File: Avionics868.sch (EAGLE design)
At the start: 60 parts, among them SW1 SPST_TACT-KMR2, U1 ATSAMD21G18_QFN, U2 SPX3819M5-L-3-0, U3 MCP73831T-2ACI/OT, U4 MPU-9250, U5 SIM868, U6 BMP180, X1 JSTPH, X2 32.768, X3 microUSB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

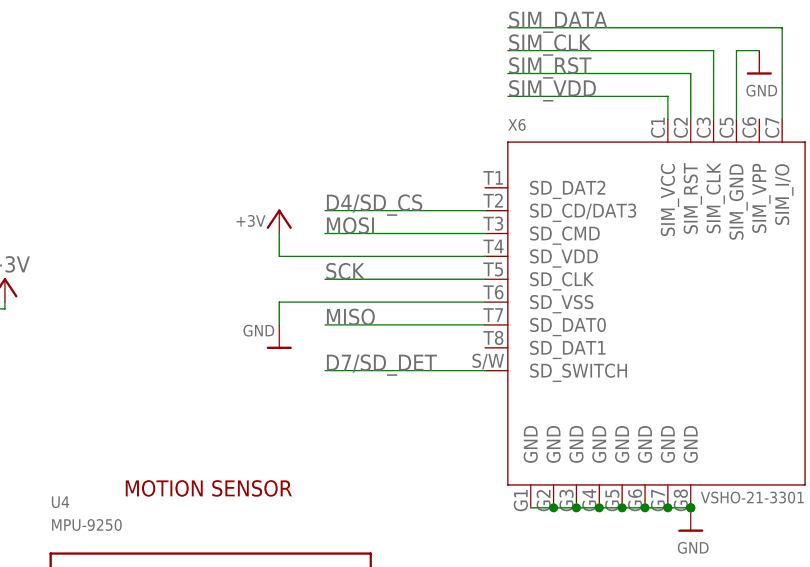
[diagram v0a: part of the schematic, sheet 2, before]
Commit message: Fixed unconnected microsd chip-select
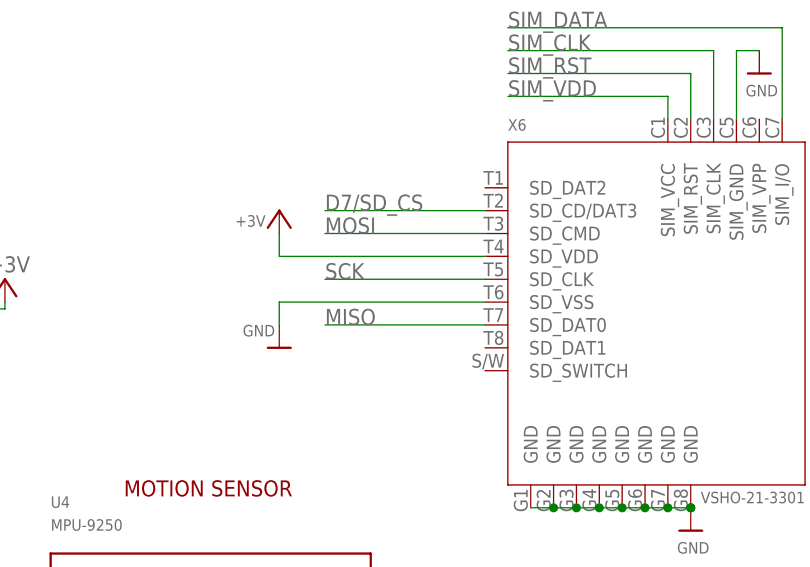
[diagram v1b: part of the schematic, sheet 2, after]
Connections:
- removed net D4/SD_CS: X6.SD_CD/DAT3
- removed net D7/SD_DET: U1.PA21/I5/SERCOM3+5.3/I2SFS0, X6.SD_SWITCH
- new net D7/SD_CS: U1.PA21/I5/SERCOM3+5.3/I2SFS0, X6.SD_CD/DAT3
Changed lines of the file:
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@@
 </segment>
 </net>
-<net name="D7/SD_DET" class="0">
+<net name="D7/SD_CS" class="0">
 <segment>
 <pinref part="U1" gate="G$1" pin="PA21/I5/SERCOM3+5.3/I2SFS0"/>
@@
 </segment>
 </net>
-<net name="D7/SD_DET" class="0">
-<segment>
-<pinref part="X6" gate="G$1" pin="SD_SWITCH"/>
-<wire x1="91.44" y1="83.82" x2="73.66" y2="83.82" width="0.1524" layer="91"/>
-<label x="73.66" y="83.82" size="1.778" layer="95"/>
-</segment>
-</net>
-<net name="D4/SD_CS" class="0">
+<net name="D7/SD_CS" class="0">
 <segment>
 <pinref part="X6" gate="G$1" pin="SD_CD/DAT3"/>

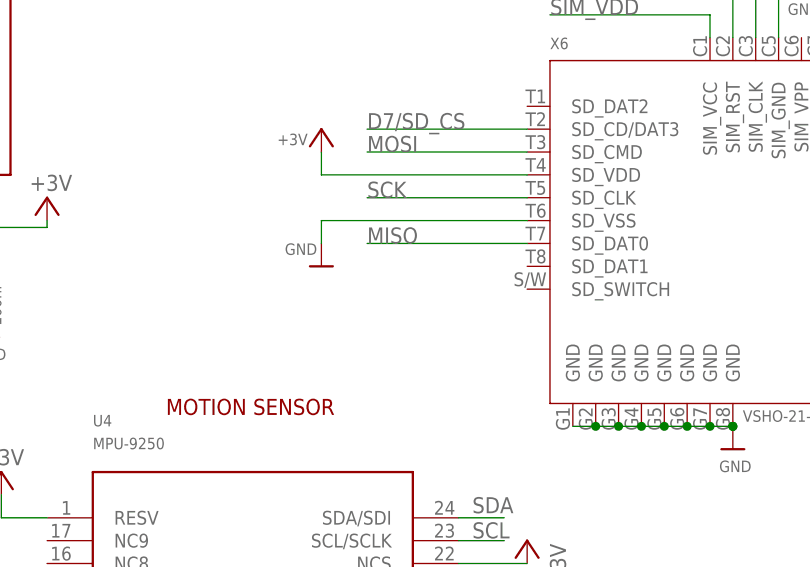
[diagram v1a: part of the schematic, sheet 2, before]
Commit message: Prev. commit was faulty, only half fixed Also fixed a number of ERC/DRC issues
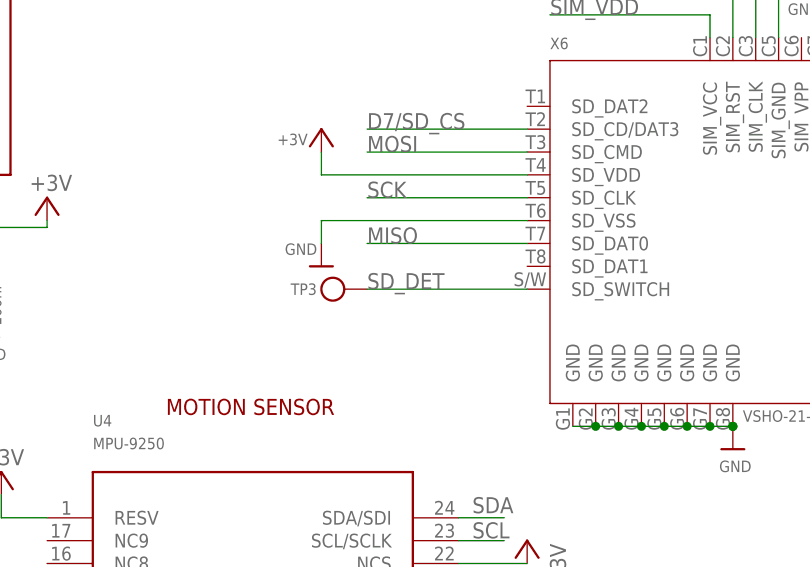
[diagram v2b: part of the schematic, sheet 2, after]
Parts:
- added TP3: (no value), microbuilder:TESTPOINTROUND1.5MM
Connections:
- new net SD_DET: TP3.P$1, X6.SD_SWITCH
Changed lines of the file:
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@@
 <part name="U$2" library="microbuilder" deviceset="VBAT" device=""/>
 <part name="GND13" library="supply1" deviceset="GND" device=""/>
+<part name="TP3" library="microbuilder" deviceset="TESTPOINT" device="ROUND1.5MM"/>
 </parts>
 <sheets>
@@
 <attribute name="VALUE" x="251.968" y="117.729" size="1.27" layer="95" align="center-left"/>
 </instance>
+<instance part="TP3" gate="G$1" x="73.66" y="83.82" rot="R90"/>
 </instances>
 <busses>
@@
 </segment>
 </net>
+<net name="SD_DET" class="0">
+<segment>
+<pinref part="X6" gate="G$1" pin="SD_SWITCH"/>
+<wire x1="91.44" y1="83.82" x2="73.66" y2="83.82" width="0.1524" layer="91"/>
+<pinref part="TP3" gate="G$1" pin="P$1"/>
+<label x="73.66" y="83.82" size="1.778" layer="95"/>
+</segment>
+</net>

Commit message: Added libraries
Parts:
- L3: value ORANGE -> BLUE
- renumbered CHG to L3, L to L1
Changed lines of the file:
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@@
 <part name="GND1" library="supply1" deviceset="GND" device=""/>
 <part name="GND12" library="supply1" deviceset="GND" device=""/>
-<part name="L" library="microbuilder" deviceset="LED" device="0805_NOOUTLINE" value="RED"/>
+<part name="L1" library="microbuilder" deviceset="LED" device="0805_NOOUTLINE" value="RED"/>
 <part name="GND7" library="supply1" deviceset="GND" device=""/>
 <part name="C14" library="microbuilder" deviceset="CAP_CERAMIC" device="0603_NO" value="1uF"/>
@@
 <part name="JP3" library="microbuilder" deviceset="HEADER-1X12" device=""/>
 <part name="U3" library="microbuilder" deviceset="MCP73831/2" device="" value="MCP73831T-2ACI/OT"/>
-<part name="CHG" library="microbuilder" deviceset="LED" device="0805_NOOUTLINE" value="ORANGE"/>
+<part name="L3" library="microbuilder" deviceset="LED" device="0805_NOOUTLINE" value="BLUE"/>
 <part name="R2" library="microbuilder" deviceset="RESISTOR" device="_0603_NOOUT" value="1K"/>
 <part name="C3" library="microbuilder" deviceset="CAP_CERAMIC" device="0805-NOOUTLINE" value="10µF"/>
@@
 <instance part="GND1" gate="1" x="167.64" y="99.06"/>
 <instance part="GND12" gate="1" x="83.82" y="127" rot="MR0"/>
-<instance part="L" gate="G$1" x="246.38" y="50.8" rot="R270"/>
+<instance part="L1" gate="G$1" x="246.38" y="50.8" rot="R270"/>
 <instance part="GND7" gate="1" x="129.54" y="144.78"/>
 <instance part="C14" gate="G$1" x="83.82" y="137.16"/>
@@
 <instance part="JP3" gate="G$1" x="180.34" y="66.04"/>
 <instance part="U3" gate="G$1" x="187.96" y="144.78"/>
-<instance part="CHG" gate="G$1" x="154.94" y="142.24"/>
+<instance part="L3" gate="G$1" x="154.94" y="142.24"/>
 <instance part="R2" gate="G$1" x="165.1" y="142.24"/>
 <instance part="C3" gate="G$1" x="220.98" y="139.7"/>
@@
 </segment>
 <segment>
-<pinref part="L" gate="G$1" pin="C"/>
+<pinref part="L1" gate="G$1" pin="C"/>
 <pinref part="GND10" gate="1" pin="GND"/>
 <wire x1="246.38" y1="48.26" x2="246.38" y2="45.72" width="0.1524" layer="91"/>
@@
 <wire x1="139.7" y1="147.32" x2="147.32" y2="147.32" width="0.1524" layer="91"/>
 <wire x1="147.32" y1="147.32" x2="175.26" y2="147.32" width="0.1524" layer="91"/>
-<pinref part="CHG" gate="G$1" pin="A"/>
+<pinref part="L3" gate="G$1" pin="A"/>
 <wire x1="149.86" y1="142.24" x2="147.32" y2="142.24" width="0.1524" layer="91"/>
 <wire x1="147.32" y1="142.24" x2="147.32" y2="147.32" width="0.1524" layer="91"/>
@@
 <net name="N$2" class="0">
 <segment>
-<pinref part="L" gate="G$1" pin="A"/>
+<pinref part="L1" gate="G$1" pin="A"/>
 <pinref part="R7" gate="G$1" pin="2"/>
 <wire x1="246.38" y1="58.42" x2="246.38" y2="55.88" width="0.1524" layer="91"/>
@@
 <net name="N$1" class="0">
 <segment>
-<pinref part="CHG" gate="G$1" pin="C"/>
+<pinref part="L3" gate="G$1" pin="C"/>
 <pinref part="R2" gate="G$1" pin="1"/>
 <wire x1="157.48" y1="142.24" x2="160.02" y2="142.24" width="0.1524" layer="91"/>

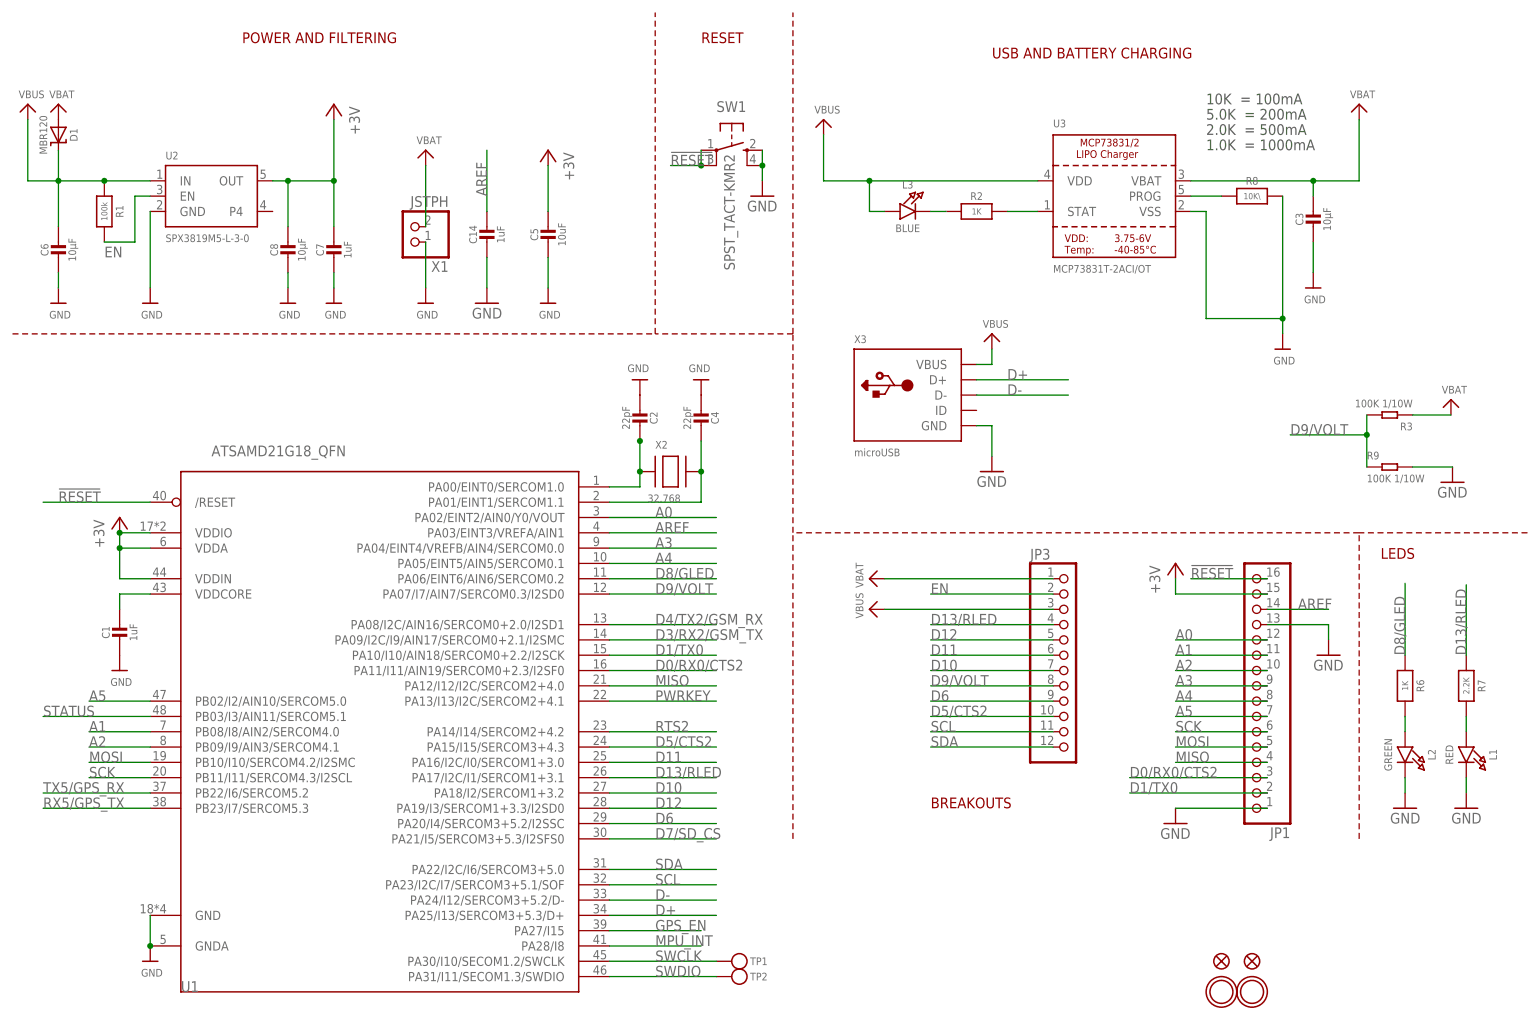
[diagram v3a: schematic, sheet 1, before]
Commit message: Added bypass capacitors ++
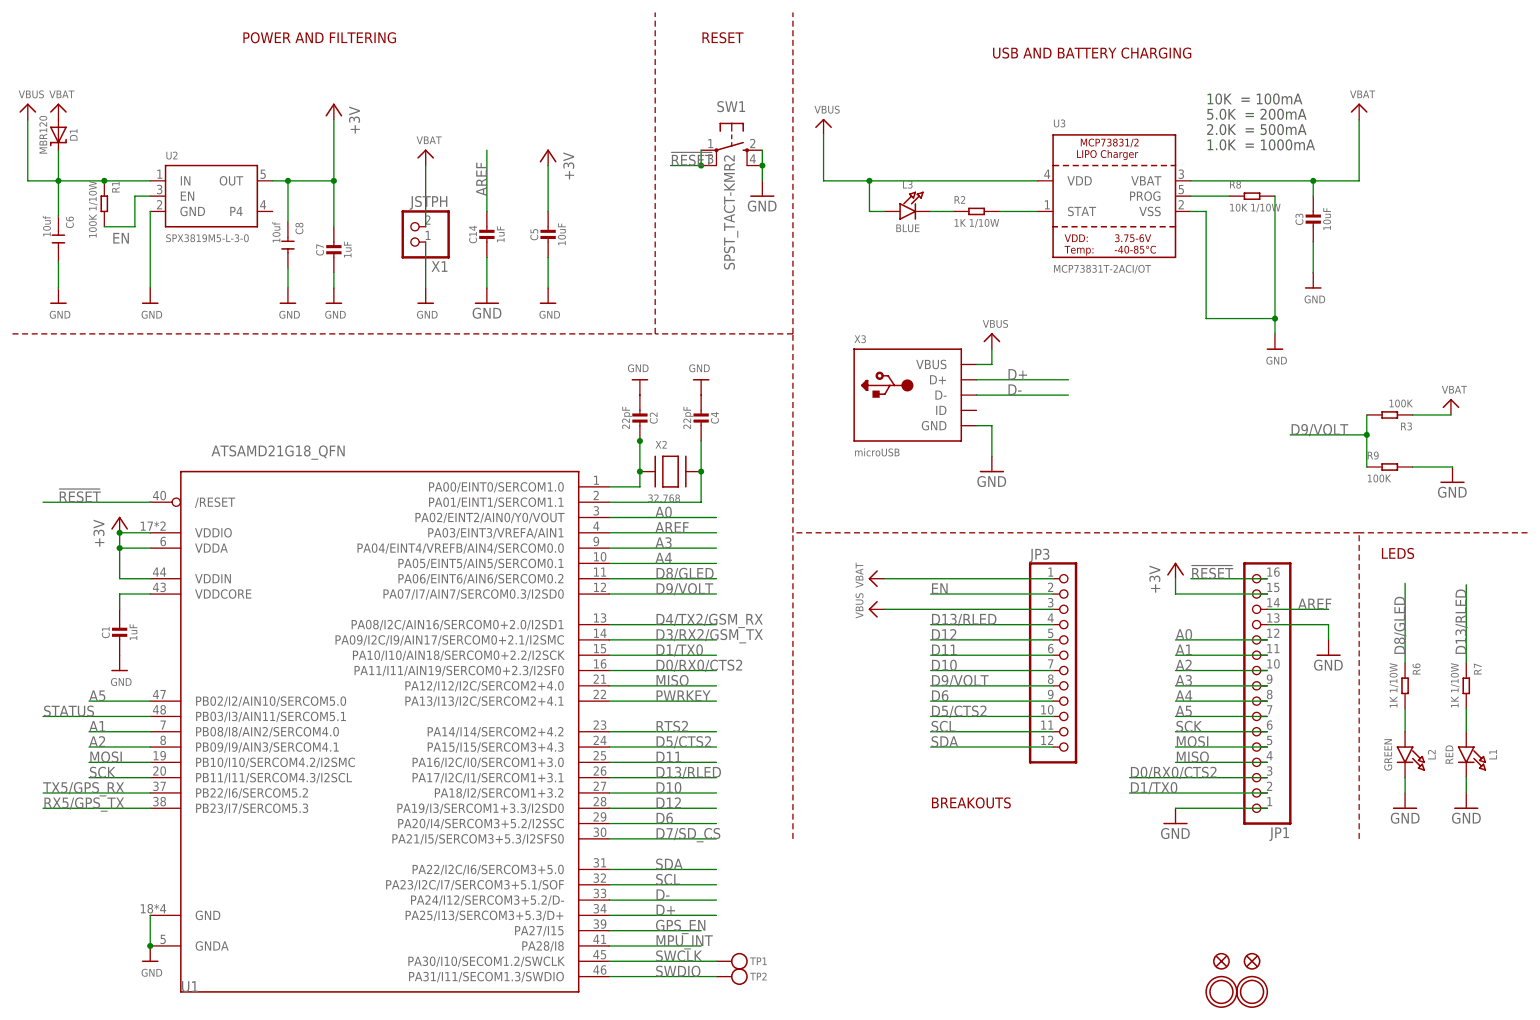
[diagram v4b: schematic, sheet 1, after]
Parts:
- added C20, C21: 10uf, Seeed-Capacitor-2016:CERAMIC-10UF-10V-10%-X5R(0603)
- C3: value 10µF -> 10uF
- C6, C8: value 10µF -> 10uf; device microbuilder:CAP_CERAMIC0805-NOOUTLINE -> Seeed-Capacitor-2016:CERAMIC-10UF-10V-10%-X5R(0603)
- R1: value 100k -> 100K 1/10W; device microbuilder:RESISTOR_0603_NOOUT -> Seeed-Resistor-2016:SMD-RES-100K-5%-1/10W(0603)
- R2, R6: value 1K -> 1K 1/10W; device microbuilder:RESISTOR_0603_NOOUT -> Seeed-Resistor-2016:SMD-RES-1K-5%-1/10W(0603)
- R3, R9: value 100K 1/10W -> 100K; device Seeed-Resistor-2016:SMD-RES-100K-5%-1/10W(0603) -> Seeed-Resistor-2016:SMD-RES-100K-1%-1/16W(0402)
- R7: value 2.2K -> 1K 1/10W; device microbuilder:RESISTOR_0603_NOOUT -> Seeed-Resistor-2016:SMD-RES-1K-5%-1/10W(0603)
- R8: value 10K\ -> 10K 1/10W; device microbuilder:RESISTOR_0603_NOOUT -> Seeed-Resistor-2016:SMD-RES-10K-5%-1/10W(0603)
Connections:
- net +3V: now also C20.1, C21.1
- net GND: now also C20.2, C21.2
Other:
- moved on the sheet: R1
